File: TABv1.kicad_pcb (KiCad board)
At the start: 4 copper layers, 90 x 45 mm, 127 parts, among them IC1 TPS630702RNMR, J1 USB_C_Receptacle_USB2.0_16P, J11 Conn_UART_1, J13 Conn_ADC, J14 Conn_BATT, J15 DB141R-2.54-8P-GN, J2 Conn_02x03_Row_Letter_Last, J3 Conn_02x03_Row_Letter_Last, J4 Conn_Coaxial, J6 SWD, J7 503398-1892, J8 Conn_SPI1, J9 Conn_SPI0, Q1 MJD44H11T4G, Q10 PJM09P30DF, Q11 PJM09P30DF, Q12 PJM09P30DF, Q13 PJM09P30DF, Q2 NMOS, Q5 NMOS, Q6 NMOS, Q7 NMOS, Q8 NMOS, Q9 NMOS, SW1 BOOTSEL, SW2 RESET, U1 RP2350B-QFN80, U10 RAK3172, U11 LPS22DF, U2 W25Q128JVS, U4 LSM6DSO32TR, U6 LT3092xST, U7 LSM6DSO32TR, U8 LIS2MDL, U9 TESEO-LIV4F, Y1 12MHz

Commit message: fix continuo
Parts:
- J11: footprint Connector_PinHeader_2.54mm:PinHeader_1x02_P2.54mm_Vertical -> Connector_JST:JST_XH_S2B-XH-A-1_1x02_P2.50mm_Horizontal
- moved LS1 28.1 mm to (86.7, 39.3)
- moved R12 22.1 mm to (143.8, 71.0), turned to 0 degrees
- moved R14 19.9 mm to (147.8, 71.0), turned to 0 degrees
- moved Q6 17.7 mm to (144.8, 74.0), turned to 0 degrees
- moved R28 15.4 mm to (148.8, 74.0), turned to 90 degrees
- moved R27 15.3 mm to (143.8, 77.0), turned to 180 degrees
- moved Q10 14.2 mm to (150.7, 76.2), turned to 0 degrees
- moved J11 11.1 mm to (43.8, 48.2), turned to -90 degrees

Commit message: upload routing con rotellini
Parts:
- removed J13: Conn_ADC, Connector_PinHeader_2.54mm:PinHeader_1x04_P2.54mm_Vertical
- removed J8: Conn_SPI1, Connector_PinHeader_2.54mm:PinHeader_1x04_P2.54mm_Vertical
- added J5: Conn_02x06_Counter_Clockwise, Connector_PinHeader_2.54mm:PinHeader_2x06_P2.54mm_Vertical, B.Cu at (106.9, 38.3)
- J11: footprint Connector_JST:JST_XH_S2B-XH-A-1_1x02_P2.50mm_Horizontal -> Connector_JST:JST_XH_B3B-XH-AM_1x03_P2.50mm_Vertical; moved to B.Cu
- J2, J3: moved to B.Cu
- moved J11 46.6 mm to (89.0, 36.8), turned to 180 degrees
- moved J6 46.6 mm to (79.2, 56.2)
- moved LS1 33.2 mm to (119.5, 44.5)
- moved Q5 10.6 mm to (134.8, 47.5)
- moved R18 10.6 mm to (138.0, 48.2)
- moved R19 10.6 mm to (138.0, 44.2)
- moved R13 10.6 mm to (131.5, 44.2)
- moved R29 10.6 mm to (134.8, 43.2)
- moved R2 10.5 mm to (103.3, 46.5)
- moved R3 10.4 mm to (107.2, 46.5)
- moved C4 6.52 mm to (109.8, 42.9), turned to 90 degrees
- moved R1 5.28 mm to (103.3, 52.0), turned to 0 degrees
- moved Q10 5.14 mm to (149.7, 71.2), turned to 90 degrees
- moved J3 4.97 mm to (155.3, 51.0)
- moved Q6 4.93 mm to (149.6, 75.2), turned to -90 degrees
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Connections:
- J11 pad 1: Net-(J11-Pin_1) -> -BATT
- U1 pad 25: Net-(J8-Pin_4) -> /GPIO24
- U1 pad 26: Net-(J8-Pin_3) -> /GPIO25
- U1 pad 27: Net-(J8-Pin_2) -> /GPIO26
- U1 pad 28: Net-(J8-Pin_1) -> /GPIO27
- U1 pad 36: /L_RED -> /GPIO28
- U1 pad 52: Net-(J13-Pin_4) -> /GPIO41
- U1 pad 53: Net-(J13-Pin_3) -> /GPIO42
- U1 pad 54: Net-(J13-Pin_2) -> /GPIO43
- U1 pad 55: Net-(J13-Pin_1) -> /GPIO44
- U1 pad 6: Net-(J11-Pin_2) -> Net-(J11-Pin_3)
- U1 pad 7: Net-(J11-Pin_1) -> Net-(J11-Pin_2)
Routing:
- net /SD_DAT0: track 52.6 -> 29.4 mm
- net Net-(Q10-G): track 0.00 -> 12.8 mm
- net /Pyro/PYRO1: track 0.00 -> 6.42 mm
- net -BATT: track 84.6 -> 79.7 mm, vias 38 -> 37
- net Net-(Q6-D): track 0.00 -> 4.42 mm
- net /Pyro/PYRO_HIGH: track 0.00 -> 4.01 mm
- net Net-(Q6-G): track 0.00 -> 3.91 mm
- net /SS: track 21.1 -> 24.5 mm, vias 2 -> 3
- net Net-(Q6-S): track 0.00 -> 2.71 mm
- net +3V3: track 87.2 -> 84.8 mm, vias 17 -> 16
- net Net-(Q7-G): track 0.00 -> 2.22 mm
- net /SD1: track 19.5 -> 20.6 mm
- net /SD2: track 17.9 -> 19.0 mm

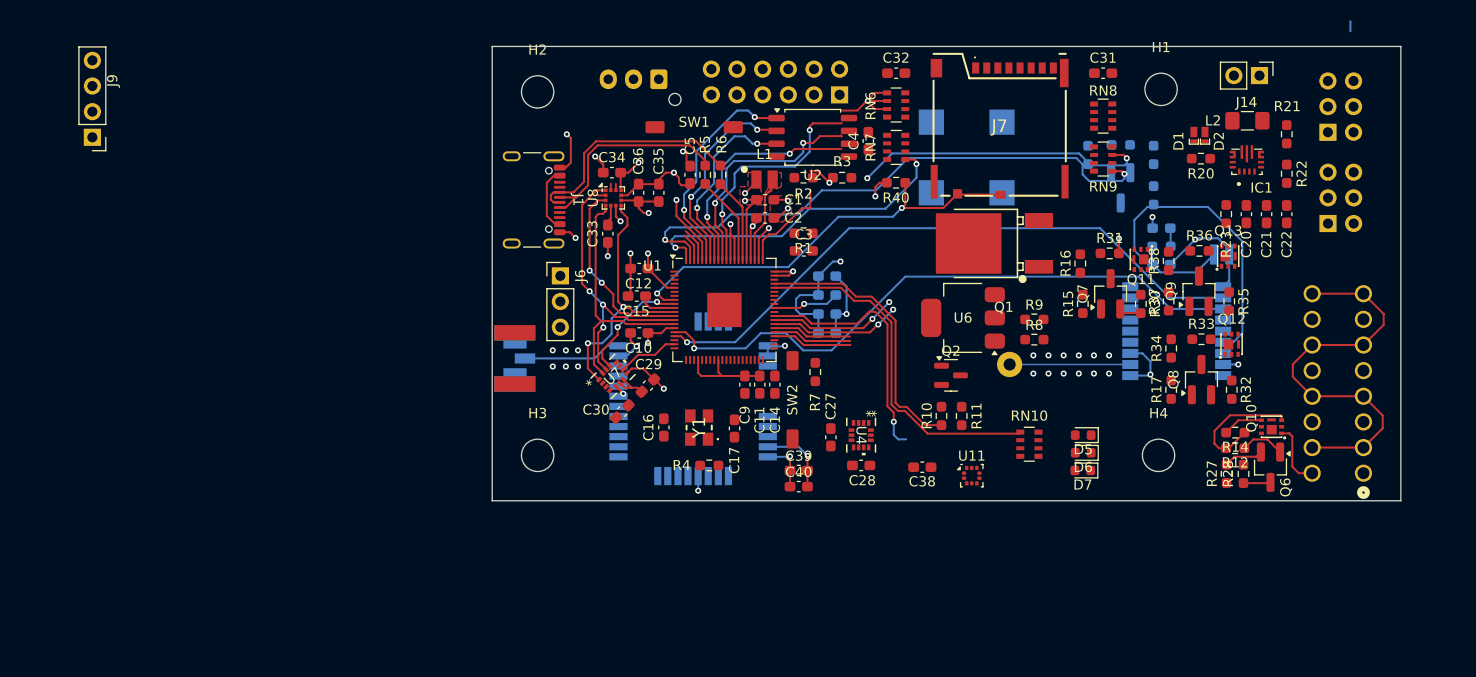
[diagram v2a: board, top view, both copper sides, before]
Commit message: Ulteriori modifiche routing
Idea di layout pyro
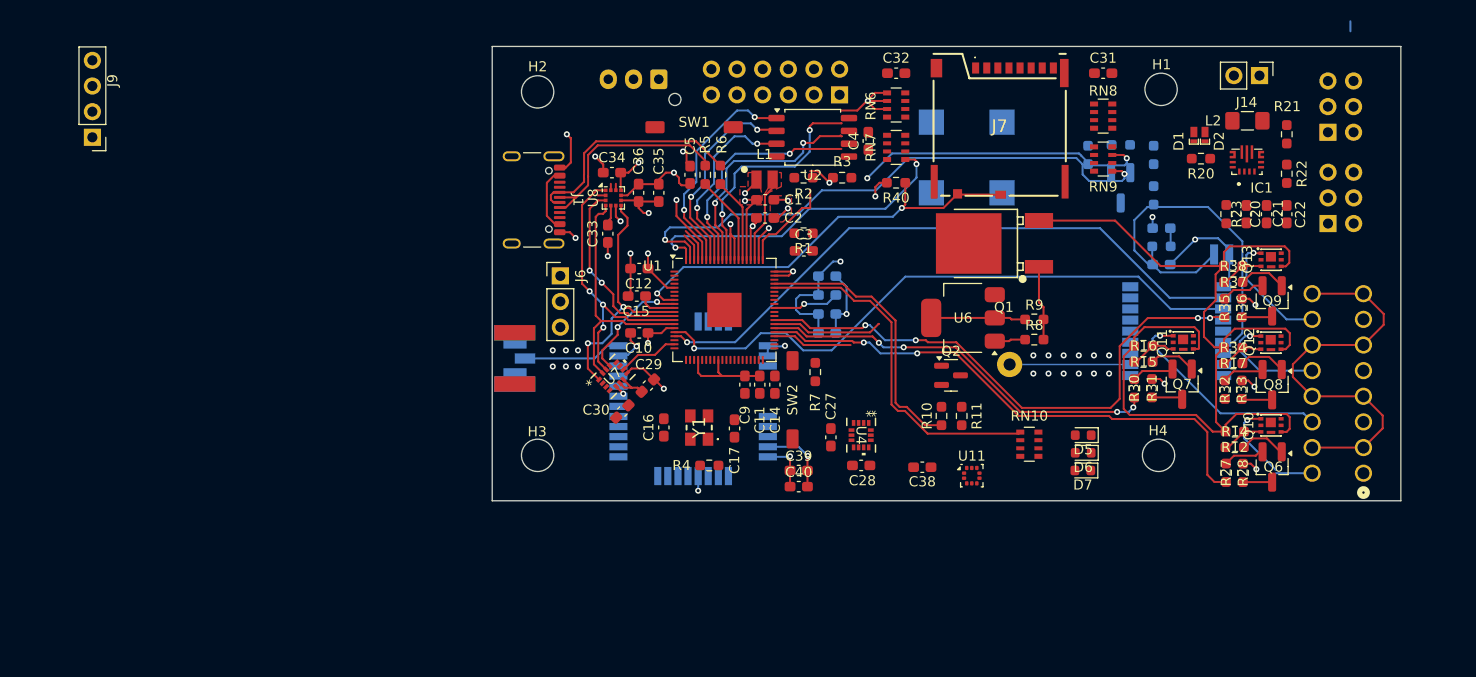
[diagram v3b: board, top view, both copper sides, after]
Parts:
- moved R31 14.0 mm to (137.8, 67.3), turned to -90 degrees
- moved Q7 11.4 mm to (140.8, 67.0), turned to -90 degrees
- moved R16 10.3 mm to (137.0, 63.1), turned to 180 degrees
- moved Q11 9.25 mm to (140.9, 62.8), turned to -90 degrees
- moved R30 8.39 mm to (136.1, 67.4), turned to 90 degrees
- moved R15 8.31 mm to (137.0, 64.8), turned to 180 degrees
- moved Q9 7.31 mm to (149.8, 58.7), turned to -90 degrees
- moved R36 7.04 mm to (146.8, 59.4), turned to -90 degrees
- moved Q8 7.02 mm to (149.8, 67.0), turned to -90 degrees
- moved R37 6.69 mm to (145.9, 56.9), turned to 180 degrees
- moved R17 6.67 mm to (145.9, 64.9), turned to 180 degrees
- moved R38 6.41 mm to (145.9, 55.2), turned to 180 degrees
- moved R33 6.40 mm to (146.8, 67.5), turned to -90 degrees
- moved R34 6.14 mm to (145.9, 63.3), turned to 180 degrees
- moved Q13 4.26 mm to (149.7, 54.6), turned to -90 degrees
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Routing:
- net /Pyro/PYRO_HIGH: track 4.01 -> 97.6 mm
- net /PYRO_FIRE_1: track 7.89 -> 53.5 mm, vias 0 -> 2
- net /PYRO_FIRE_4: track 12.8 -> 55.2 mm, vias 2 -> 4
- net /PYRO_FIRE_2: track 7.82 -> 40.2 mm, vias 0 -> 4
- net /PYRO_SENSE: track 25.1 -> 0.00 mm, vias 1 -> 0
- net /Pyro/PYRO2: track 0.00 -> 21.8 mm, vias 0 -> 1
- net /Pyro/PYRO4: track 0.00 -> 12.1 mm, vias 0 -> 1
- net /Pyro/PYRO3: track 0.00 -> 11.2 mm, vias 0 -> 1
- net Net-(R9-Pad1): track 0.00 -> 9.36 mm
- net Net-(Q10-G): track 12.8 -> 4.17 mm
- net Net-(Q1-B): track 0.00 -> 7.40 mm
- net Net-(Q11-G): track 0.00 -> 5.09 mm
- net /Pyro/PYRO1: track 6.42 -> 11.4 mm, vias 0 -> 1
- net Net-(Q9-D): track 0.00 -> 4.77 mm
- net Net-(Q8-D): track 0.00 -> 4.68 mm
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
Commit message: Changes meeting 03/12
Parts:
- removed J14: Conn_BATT, Connector_PinHeader_2.54mm:PinHeader_1x02_P2.54mm_Vertical
- removed J9: Conn_SPI0, Connector_PinHeader_2.54mm:PinHeader_1x04_P2.54mm_Vertical
- added J8: 1053141104, footprints:CONN_SD-105314-100_04_MOL, F.Cu at (151.8, 39.4)
- added R41: 10k, Resistor_SMD:R_0603_1608Metric_Pad0.98x0.95mm_HandSolder, F.Cu at (145.2, 36.2)
- added R42: 40k, Resistor_SMD:R_0603_1608Metric_Pad0.98x0.95mm_HandSolder, F.Cu at (147.8, 36.2)
- Q5, R13, R18, R19, R29: moved to F.Cu
- moved R13 12.8 mm to (139.7, 54.0)
- moved R18 10.9 mm to (133.2, 58.0)
- moved R19 10.9 mm to (133.2, 54.0)
- moved Q5 9.91 mm to (136.5, 57.2)
- moved R29 9.90 mm to (136.5, 53.0), turned to 0 degrees
- moved J2 9.27 mm to (153.2, 51.0)
- moved L2 3.71 mm to (143.6, 40.7)
- moved D1 3.71 mm to (138.3, 42.1)
- moved D2 3.71 mm to (139.4, 42.1)
- moved R21 3.71 mm to (147.5, 42.0)
- moved C20 3.71 mm to (143.5, 49.9)
- moved C21 3.71 mm to (145.5, 49.9)
- moved C22 3.71 mm to (147.5, 49.9)
- moved IC1 3.71 mm to (143.6, 45.3)
- moved R20 3.71 mm to (139.0, 44.4)
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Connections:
- net -BATT renamed GND
- J5 pad 3: /GPIO24 -> /GPIO20
- J5 pad 5: /GPIO25 -> /GPIO21
- J5 pad 7: /GPIO26 -> /GPIO22
- J5 pad 9: /GPIO27 -> /GPIO23
- U1 pad 20: /PWM1 -> /GPIO20
- U1 pad 21: /PWM2 -> /GPIO21
- U1 pad 22: /PWM3 -> /GPIO22
- U1 pad 23: /PWM4 -> /GPIO23
- U1 pad 25: /GPIO24 -> /PWM1
- U1 pad 26: /GPIO25 -> /PWM2
- U1 pad 27: /GPIO26 -> /PWM3
- U1 pad 28: /GPIO27 -> /PWM4
- U1 pad 58: unconnected-(U1-GPIO47_ADC7-Pad58) -> /BATT_SENSE
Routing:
- net /PYRO_FIRE_4: track 55.2 -> 0.00 mm, vias 4 -> 0
- net /Pyro/PYRO_HIGH: track 97.6 -> 62.5 mm, vias 0 -> 2
- added copper zone on In2.Cu, net /Pyro/PYRO_HIGH

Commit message: ultime change routing pyro
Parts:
- moved R32 5.08 mm to (146.0, 62.5), turned to 0 degrees
- moved Q12 4.34 mm to (150.6, 67.1), turned to 180 degrees
- moved R34 4.21 mm to (150.1, 63.4), turned to 90 degrees
- moved Q13 3.65 mm to (146.0, 54.5)
- moved R33 3.34 mm to (146.0, 64.2), turned to 180 degrees
- moved R38 3.28 mm to (143.5, 57.5), turned to -90 degrees
- moved Q8 3.25 mm to (146.5, 67.0), turned to 180 degrees
- moved R17 3.05 mm to (148.5, 63.4), turned to 90 degrees
- moved R35 1.99 mm to (147.0, 59.0)
- moved R36 1.55 mm to (145.2, 59.0)
- moved R37 0.36 mm to (146.0, 56.5)
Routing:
- net /Pyro/PYRO_HIGH: track 62.5 -> 46.4 mm, vias 2 -> 5
- net /Pyro/PYRO3: track 11.2 -> 2.68 mm, vias 1 -> 0
- net /PYRO_FIRE_4: track 0.00 -> 5.41 mm
- net Net-(Q9-S): track 3.05 -> 5.27 mm
- net GND: track 78.5 -> 80.7 mm
- net Net-(Q9-G): track 4.28 -> 2.17 mm
- net /Pyro/PYRO4: track 12.1 -> 13.8 mm, vias 1 -> 0
- net Net-(Q13-G): track 4.33 -> 3.39 mm

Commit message: wiring parte pyro
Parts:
- moved U6 18.3 mm to (136.0, 53.4), turned to 0 degrees
- moved R8 12.1 mm to (130.8, 51.4), turned to 90 degrees
- moved R20 10.3 mm to (147.6, 38.8)
- moved R29 8.89 mm to (142.8, 59.2), turned to -90 degrees
- moved Q13 8.68 mm to (150.7, 61.8), turned to 180 degrees
- moved R9 7.36 mm to (130.8, 54.8), turned to -90 degrees
- moved C21 7.05 mm to (148.2, 43.4), turned to 0 degrees
- moved R38 6.53 mm to (150.0, 58.1), turned to 90 degrees
- moved Q11 5.87 mm to (141.6, 68.7), turned to 180 degrees
- moved R19 5.84 mm to (135.9, 59.2), turned to 90 degrees
- moved R13 5.42 mm to (141.2, 59.2), turned to 90 degrees
- moved R16 5.25 mm to (141.8, 65.2), turned to 90 degrees
- moved Q10 5.02 mm to (150.8, 76.0), turned to 180 degrees
- moved R14 4.52 mm to (150.5, 72.5), turned to 90 degrees
- moved Q9 4.42 mm to (146.5, 61.7), turned to 180 degrees
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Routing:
- net /PYRO_FIRE_3: track 11.0 -> 46.1 mm, vias 0 -> 2
- net /Pyro/PYRO_HIGH: track 46.4 -> 13.0 mm, vias 5 -> 7
- net /PYRO_SENSE: track 0.00 -> 19.2 mm
- net /Pyro/PYRO_LOW: track 40.5 -> 58.1 mm
- net +BATT: track 0.00 -> 13.9 mm
- net GND: track 80.7 -> 93.4 mm, vias 39 -> 40
- net /Pyro/PYRO4: track 13.8 -> 2.40 mm
- net /Pyro/PYRO1: track 11.4 -> 2.63 mm, vias 1 -> 0
- net /Pyro/PYRO2: track 21.8 -> 13.4 mm
- net /PYRO_ENABLE: track 7.91 -> 13.4 mm
- net /PYRO_FIRE_4: track 5.41 -> 0.00 mm
- net /SD0: track 22.8 -> 17.5 mm
- net /PYRO_FIRE_1: track 53.5 -> 49.0 mm
- net Net-(Q5-G): track 0.00 -> 3.62 mm
- net /SS: track 24.5 -> 21.5 mm, vias 3 -> 2
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
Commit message: minor_changes
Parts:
- moved D5 26.1 mm to (114.0, 52.2)
- moved D6 26.1 mm to (114.0, 54.0)
- moved D7 26.1 mm to (114.0, 55.8)
- moved RN10 23.9 mm to (110.9, 54.1)
- moved R10 19.6 mm to (107.2, 87.0)
- moved R11 19.6 mm to (109.2, 87.0)
- moved Q2 19.6 mm to (108.1, 83.0)
- moved U11 13.8 mm to (108.4, 68.6)
- moved C38 6.24 mm to (109.2, 77.2)
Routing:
- net /L_BLUE: track 35.2 -> 0.21 mm
- net /BUZZ: track 27.1 -> 0.00 mm
- net GND: track 93.4 -> 102.4 mm
- net /Pyro/PYRO4: track 2.40 -> 7.48 mm
- net /Pyro/PYRO1: track 2.63 -> 7.71 mm
- net /Pyro/PYRO2: track 13.4 -> 18.5 mm
- net /PYRO_FIRE_2: track 42.6 -> 41.8 mm
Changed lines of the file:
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@@
 			(psa4output no)
 			(plot_black_and_white yes)
-			(plotinvisibletext no)
 			(sketchpadsonfab no)
 			(plotpadnumbers no)
@@
 	(footprint "Resistor_SMD:R_0603_1608Metric_Pad0.98x0.95mm_HandSolder"
 		(layer "F.Cu")
-		(at 117 70.1 90)
+		(at 107.1575 87.025 90)
 		(descr "Resistor SMD 0603 (1608 Metric), square (rectangular) end terminal, IPC_7351 nominal with elongated pad for handsoldering. (Body size source: IPC-SM-782 page 72, https://www.pcb-3d.com/wordpress/wp-content/uploads/ipc-sm-782a_amendment_1_and_2.pdf), generated with kicad-footprint-generator")
 		(tags "resistor handsolder")
@@
 	(footprint "LED_SMD:LED_0603_1608Metric"
 		(layer "F.Cu")
-		(at 131 75.5 180)
+		(at 113.9625 55.75 180)
 		(descr "LED SMD 0603 (1608 Metric), square (rectangular) end terminal, IPC_7351 nominal, (Body size source: http://www.tortai-tech.com/upload/download/2011102023233369053.pdf), generated with kicad-footprint-generator")
 		(tags "LED")
@@
 	(footprint "Package_TO_SOT_SMD:SOT-23"
 		(layer "F.Cu")
-		(at 117.9425 66.075)
+		(at 108.1 83)
 		(descr "SOT, 3 Pin (JEDEC TO-236 Var AB https://www.jedec.org/document_search?search_api_views_fulltext=TO-236), generated with kicad-footprint-generator ipc_gullwing_generator.py")
 		(tags "SOT TO_SOT_SMD")
@@
 	(footprint "Capacitor_SMD:C_0603_1608Metric_Pad1.08x0.95mm_HandSolder"
 		(layer "F.Cu")
-		(at 115.1 75.175 180)
+		(at 109.2 77.2 180)
 		(descr "Capacitor SMD 0603 (1608 Metric), square (rectangular) end terminal, IPC-7351 nominal with elongated pad for handsoldering. (Body size source: IPC-SM-782 page 76, https://www.pcb-3d.com/wordpress/wp-content/uploads/ipc-sm-782a_amendment_1_and_2.pdf), generated with kicad-footprint-generator")
 		(tags "capacitor handsolder")
@@
 	(footprint "Resistor_SMD:R_Array_Convex_4x0603"
 		(layer "F.Cu")
-		(at 125.7 72.9)
+		(at 110.9 54.1)
 		(descr "Chip Resistor Network, ROHM MNR14 (see mnr_g.pdf)")
 		(tags "resistor array")
@@
 	(footprint "LED_SMD:LED_0603_1608Metric"
 		(layer "F.Cu")
-		(at 131.0375 73.75 180)
+		(at 114 54 180)
 		(descr "LED SMD 0603 (1608 Metric), square (rectangular) end terminal, IPC_7351 nominal, (Body size source: http://www.tortai-tech.com/upload/download/2011102023233369053.pdf), generated with kicad-footprint-generator")
 		(tags "LED")
@@
 	(footprint "Resistor_SMD:R_0603_1608Metric_Pad0.98x0.95mm_HandSolder"
 		(layer "F.Cu")
-		(at 119 70.1 90)
+		(at 109.1575 87.025 90)
 		(descr "Resistor SMD 0603 (1608 Metric), square (rectangular) end terminal, IPC_7351 nominal with elongated pad for handsoldering. (Body size source: IPC-SM-782 page 72, https://www.pcb-3d.com/wordpress/wp-content/uploads/ipc-sm-782a_amendment_1_and_2.pdf), generated with kicad-footprint-generator")
 		(tags "resistor handsolder")
@@
 	(footprint "Package_LGA:ST_HLGA-10_2x2mm_P0.5mm_LayoutBorder3x2y"
 		(layer "F.Cu")
-		(at 120 76.0125)
+		(at 108.4 68.6)
 		(descr "ST  HLGA, 10 Pin (https://www.st.com/resource/en/datasheet/lps22hh.pdf#page=55), generated with kicad-footprint-generator ipc_noLead_generator.py")
 		(tags "ST HLGA NoLead")
@@
 	(footprint "LED_SMD:LED_0603_1608Metric"
 		(layer "F.Cu")
-		(at 131.0375 72 180)
+		(at 114 52.25 180)
 		(descr "LED SMD 0603 (1608 Metric), square (rectangular) end terminal, IPC_7351 nominal, (Body size source: http://www.tortai-tech.com/upload/download/2011102023233369053.pdf), generated with kicad-footprint-generator")
 		(tags "LED")
@@
 	)
 	(segment
+		(start 153.715301 60.529599)
+		(end 158.795301 60.529599)
+		(width 0.2)
+		(layer "F.Cu")
+		(net 45)
+	)
+	(segment
 		(start 143.25 69.689599)
 		(end 143.25 68.40625)
@@
 		(net 46)
 	)
+	(segment
+		(start 153.715301 70.689599)
+		(end 158.795301 70.689599)
+		(width 0.2)
+		(layer "F.Cu")
+		(net 46)
+	)
 	(via
 		(at 144.25 70.689599)
@@
 	)
 	(segment
+		(start 153.715301 75.769599)
+		(end 158.795301 75.769599)
+		(width 0.2)
+		(layer "F.Cu")
+		(net 47)
+	)
+	(segment
 		(start 151.42 74.95)
 		(end 152.195702 74.95)
@@
 	)
 	(segment
-		(start 118.3329 63.8)
-		(end 114.6 63.8)
+		(start 103.525 62.675)
+		(end 107.975 62.675)
 		(width 0.2)
 		(layer "F.Cu")
@@
 	)
 	(segment
-		(start 133.951 70.101)
-		(end 124.6339 70.101)
+		(start 108.1661 62.674)
+		(end 107.975 62.674)
 		(width 0.2)
 		(layer "F.Cu")
@@
 	)
 	(segment
-		(start 103.525 62.675)
-		(end 107.975 62.675)
+		(start 102.65 61.8)
+		(end 103.525 62.675)
 		(width 0.2)
 		(layer "F.Cu")
@@
 	(segment
 		(start 145.0875 71.95)
-		(end 135.8 71.95)
+		(end 136.55 71.95)
 		(width 0.2)
 		(layer "F.Cu")
@@
 	)
 	(segment
-		(start 114.6 63.8)
-		(end 114.6 63.9)
+		(start 133.7 69.1)
+		(end 123.6329 69.1)
 		(width 0.2)
 		(layer "F.Cu")
@@
 	)
 	(segment
-		(start 108.1661 62.674)
-		(end 107.975 62.674)
+		(start 100.45 61.8)
+		(end 102.65 61.8)
 		(width 0.2)
 		(layer "F.Cu")
@@
 	)
 	(segment
-		(start 102.65 61.8)
-		(end 103.525 62.675)
+		(start 114.6 63.8)
+		(end 114.6 63.9)
 		(width 0.2)
 		(layer "F.Cu")
@@
 	)
 	(segment
-		(start 100.45 61.8)
-		(end 102.65 61.8)
+		(start 136.55 71.95)
+		(end 133.7 69.1)
 		(width 0.2)
 		(layer "F.Cu")
@@
 	)
 	(segment
-		(start 124.6339 70.101)
+		(start 123.6329 69.1)
 		(end 118.3329 63.8)
 		(width 0.2)
@@
 	)
 	(segment
-		(start 135.8 71.95)
-		(end 133.951 70.101)
+		(start 118.3329 63.8)
+		(end 114.6 63.8)
 		(width 0.2)
 		(layer "F.Cu")
@@
 	)
 	(segment
-		(start 135.8375 64.15625)
-		(end 134.4 65.59375)
+		(start 134.4 68.1)
+		(end 133.8 68.7)
 		(width 0.2)
 		(layer "F.Cu")
@@
 	)
 	(segment
-		(start 124.8 69.7)
+		(start 123.8 68.7)
 		(end 118.4 63.3)
 		(width 0.2)
@@
 	)
 	(segment
-		(start 134.4 65.59375)
-		(end 134.4 68.1)
+		(start 135.8375 64.15625)
+		(end 134.4 65.59375)
 		(width 0.2)
 		(layer "F.Cu")
@@
 	)
 	(segment
-		(start 134.4 68.1)
-		(end 132.8 69.7)
+		(start 133.8 68.7)
+		(end 123.8 68.7)
 		(width 0.2)
 		(layer "F.Cu")
@@
 	)
 	(segment
-		(start 132.8 69.7)
-		(end 124.8 69.7)
+		(start 118.4 63.3)
+		(end 113.25 63.3)
 		(width 0.2)
 		(layer "F.Cu")
@@
 	)
 	(segment
-		(start 118.4 63.3)
-		(end 113.25 63.3)
+		(start 134.4 65.59375)
+		(end 134.4 68.1)
 		(width 0.2)
 		(layer "F.Cu")
@@
 	)
 	(segment
-		(start 112.85 69.2)
-		(end 113.55 69.2)
-		(width 0.2)
-		(layer "F.Cu")
-		(net 149)
-	)
-	(segment
-		(start 112.45 68.8)
-		(end 112.85 69.2)
-		(width 0.2)
-		(layer "F.Cu")
-		(net 149)
-	)
-	(segment
-		(start 108.525 58.275)
-		(end 110.075 58.275)
-		(width 0.2)
-		(layer "F.Cu")
-		(net 149)
-	)
-	(segment
-		(start 113.55 69.2)
-		(end 115.3625 71.0125)
-		(width 0.2)
-		(layer "F.Cu")
-		(net 149)
-	)
-	(segment
-		(start 115.3625 71.0125)
-		(end 117 71.0125)
-		(width 0.2)
-		(layer "F.Cu")
-		(net 149)
-	)
-	(segment
-		(start 112.45 60.65)
-		(end 112.45 68.8)
-		(width 0.2)
-		(layer "F.Cu")
-		(net 149)
-	)
-	(segment
-		(start 107.25 57)
-		(end 108.525 58.275)
-		(width 0.2)
-		(layer "F.Cu")
-		(net 149)
-	)
-	(segment
-		(start 100.45 57)
-		(end 107.25 57)
-		(width 0.2)
-		(layer "F.Cu")
-		(net 149)
-	)
-	(segment
-		(start 110.075 58.275)
-		(end 112.45 60.65)
-		(width 0.2)
-		(layer "F.Cu")
-		(net 149)
-	)
-	(segment
-		(start 124.65 71.85)
-		(end 124.8 71.7)
-		(width 0.2)
-		(layer "F.Cu")
-		(net 152)
-	)
-	(segment
-		(start 112.049 68.9661)
-		(end 112.6839 69.601)
-		(width 0.2)
-		(layer "F.Cu")
-		(net 152)
-	)
-	(segment
-		(start 112.6839 69.601)
-		(end 113.376 69.601)
-		(width 0.2)
-		(layer "F.Cu")
-		(net 152)
-	)
-	(segment
-		(start 107.05 57.4)
-		(end 108.35 58.7)
-		(width 0.2)
-		(layer "F.Cu")
-		(net 152)
-	)
-	(segment
-		(start 109.925 58.7)
-		(end 112.049 60.824)
-		(width 0.2)
-		(layer "F.Cu")
-		(net 152)
-	)
-	(segment
-		(start 108.35 58.7)
-		(end 109.925 58.7)
-		(width 0.2)
-		(layer "F.Cu")
-		(net 152)
-	)
-	(segment
-		(start 112.049 60.824)
-		(end 112.049 68.9661)
-		(width 0.2)
-		(layer "F.Cu")
-		(net 152)
-	)
-	(segment
-		(start 115.625 71.85)
-		(end 124.65 71.85)
-		(width 0.2)
-		(layer "F.Cu")
-		(net 152)
-	)
-	(segment
-		(start 113.376 69.601)
-		(end 115.625 71.85)
-		(width 0.2)
-		(layer "F.Cu")
-		(net 152)
-	)
-	(segment
-		(start 100.45 57.4)
-		(end 107.05 57.4)
+		(start 109.85 53.05)
+		(end 110 52.9)
 		(width 0.2)
 		(layer "F.Cu")
@@
 	)
 	(segment
+		(start 78.5 63.6)
+		(end 76.474 63.6)
+		(width 0.2)
+		(layer "F.Cu")
+		(net 204)
+	)
+	(segment
 		(start 86.205 54.005)
 		(end 86.2 54)
@@
 	)
 	(segment
+		(start 78.5 65.2)
+		(end 76.474 65.2)
+		(width 0.2)
+		(layer "F.Cu")
+		(net 204)
+	)
+	(segment
 		(start 83.5 46)
 		(end 83.5 45.2)
@@
 	)
 	(segment
+		(start 76.474 65.2)
+		(end 74.734 66.94)
+		(width 0.2)
+		(layer "F.Cu")
+		(net 204)
+	)
+	(segment
 		(start 137.0125 60.1125)
 		(end 138.6 61.7)
@@
 		(width 0.2)
 		(layer "F.Cu")
+		(net 204)
+	)
+	(segment
+		(start 76.474 63.6)
+		(end 74.734 61.86)
+		(width 0.2)
+		(layer "F.Cu")
